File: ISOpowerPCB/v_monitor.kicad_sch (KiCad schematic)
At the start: 26 parts, among them U15 TL431DBZ, U16 TL431DBZ, U17 TL431DBZ, U18 TL431DBZ, U19 HEF4093B

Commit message: PCB Layouts
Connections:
- net 12V_MON_OUT: no longer U19.5, U19.6
- net at D5.2 (A), U19.3: now also U19.5, U19.6; no longer U19.8, U19.9
- net at D6.2 (A), U19.12, U19.13: now also U19.10; no longer U19.4
- net at D7.2 (A): now also U19.4; no longer U19.10
- new net: U19.8, U19.9
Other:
- moved on the sheet: U19B, U19C

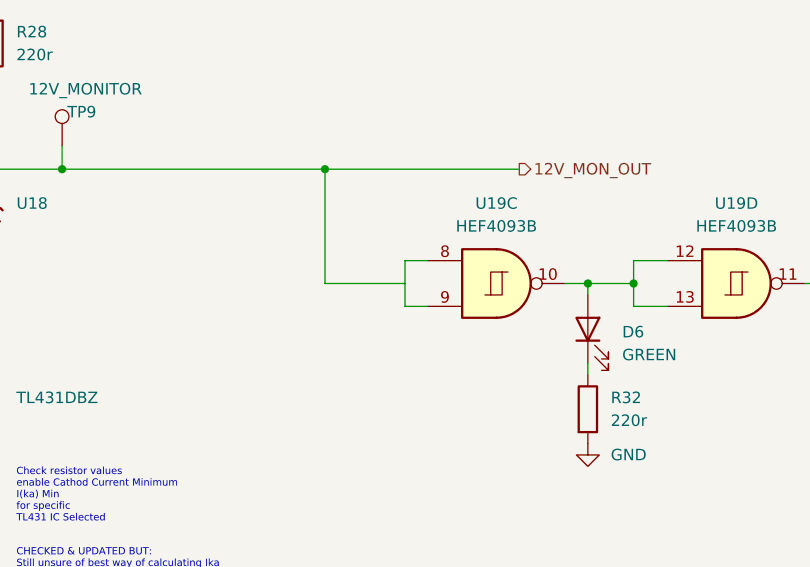
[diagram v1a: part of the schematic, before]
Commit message: Components placed V1.0
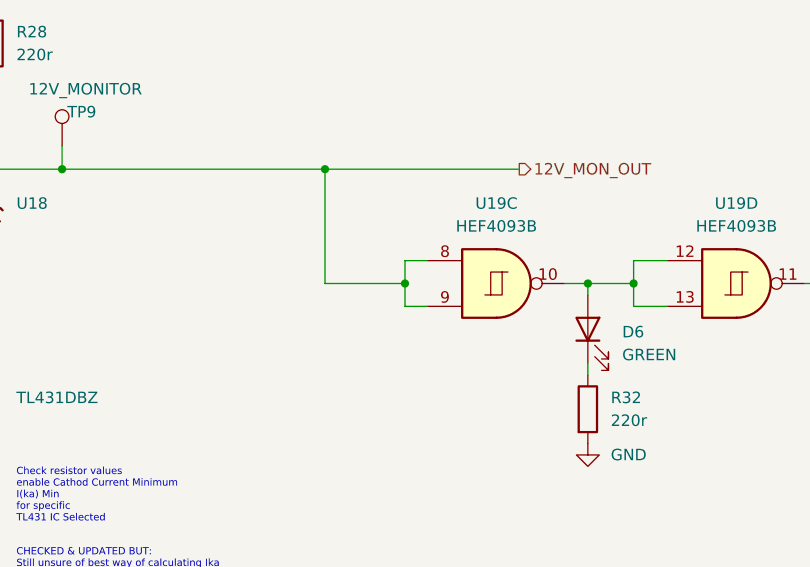
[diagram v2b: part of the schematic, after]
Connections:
- net 12V_MON_OUT: now also U19.8, U19.9
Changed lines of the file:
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@@
   (junction (at 38.1 140.97) (diameter 0) (color 0 0 0 0)
   )
+  (junction (at 119.38 143.51) (diameter 0) (color 0 0 0 0)
+  )
   (wire (pts (xy 228.6 30.48) (xy 231.14 30.48))
     (stroke (width 0) (type default) (color 0 0 0 0))
@@
     (stroke (width 0) (type default) (color 0 0 0 0))
   )
-  (wire (pts (xy 119.38 140.97) (xy 119.38 146.05))
+  (wire (pts (xy 119.38 140.97) (xy 119.38 143.51))
     (stroke (width 0) (type default) (color 0 0 0 0))
   )
@@
     (stroke (width 0) (type default) (color 0 0 0 0))
   )
+  (wire (pts (xy 119.38 143.51) (xy 119.38 146.05))
+    (stroke (width 0) (type default) (color 0 0 0 0))
+  )

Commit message: Started Routing V1
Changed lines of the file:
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@@
       (effects (font (size 1.27 1.27)) (justify right))
     )
-    (property "Value" "TL431DBZ" (id 1) (at 76.2 156.2099 90)
+    (property "Value" "TL431DBZ" (id 1) (at 76.2 137.16 90)
       (effects (font (size 1.27 1.27)) (justify right))
     )

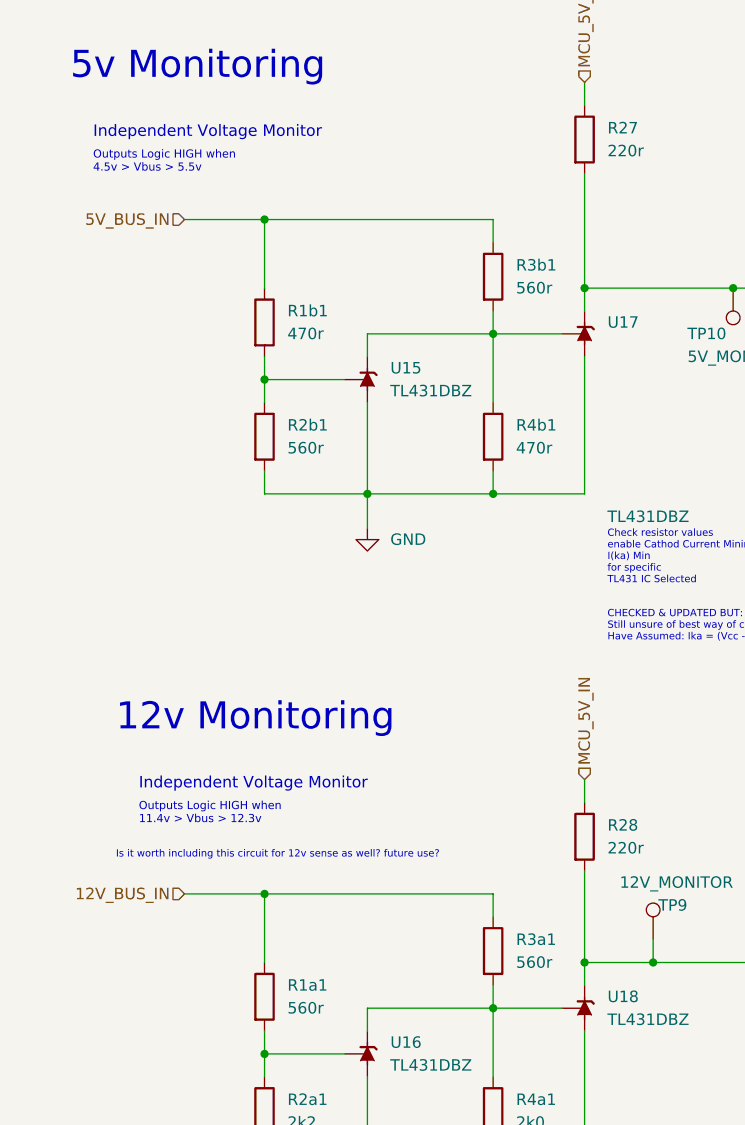
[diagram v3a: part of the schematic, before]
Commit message: Replacing power bus RE current draw issue
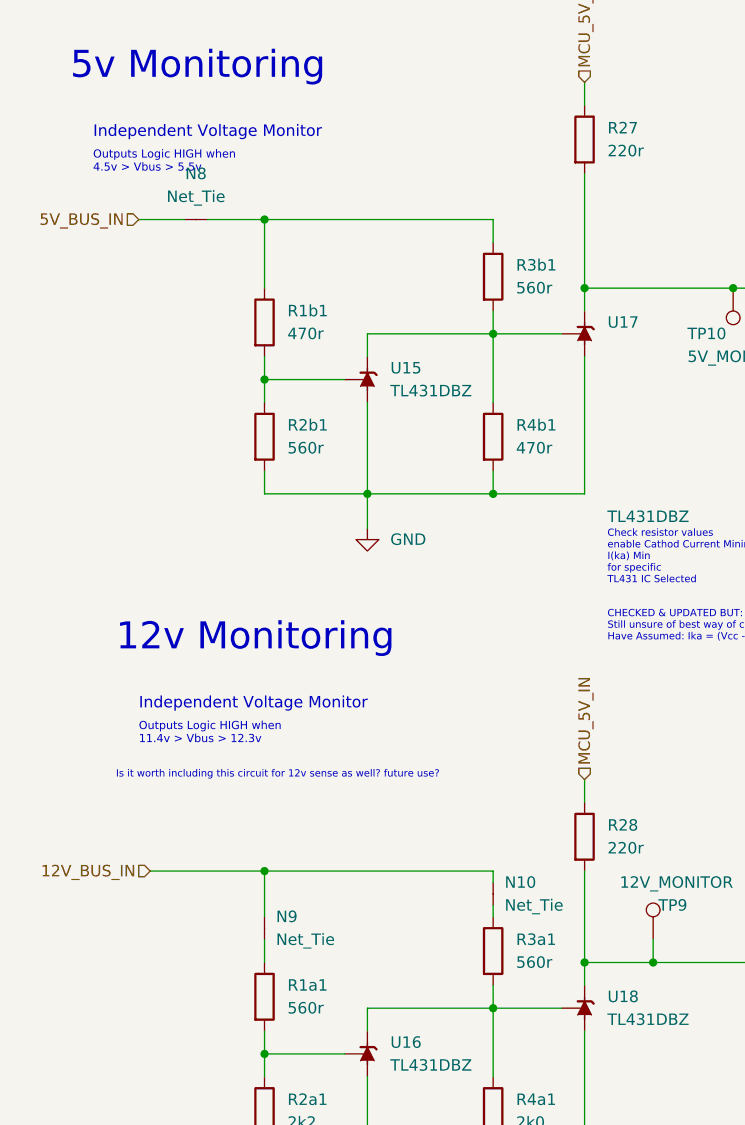
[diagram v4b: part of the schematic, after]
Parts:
- added N10, N8, N9: Net_Tie, NetTie:NetTie-2_SMD_Pad0.5mm, symbol 000_Utility_Immo:Net_Tie
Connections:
- net 12V_BUS_IN: now also N10.1 (A), N9.1 (A); no longer R1a1.1, R3a1.1
- net 5V_BUS_IN: now also N8.1 (A); no longer R1b1.1, R3b1.1
- new net: N9.2 (C), R1a1.1
- new net: N8.2 (C), R1b1.1, R3b1.1
- new net: N10.2 (C), R3a1.1
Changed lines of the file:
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@@
   (junction (at 63.5 135.89) (diameter 0) (color 0 0 0 0)
   )
-  (junction (at 38.1 123.19) (diameter 0) (color 0 0 0 0)
-  )
   (junction (at 63.5 78.74) (diameter 0) (color 0 0 0 0)
   )
@@
   (junction (at 144.78 143.51) (diameter 0) (color 0 0 0 0)
   )
+  (junction (at 38.1 120.65) (diameter 0) (color 0 0 0 0)
+  )
   (junction (at 73.66 55.88) (diameter 0) (color 0 0 0 0)
   )
+  (junction (at 130.81 67.31) (diameter 0) (color 0 0 0 0)
+  )
+  (junction (at 81.28 130.81) (diameter 0) (color 0 0 0 0)
+  )
+  (junction (at 49.53 78.74) (diameter 0) (color 0 0 0 0)
+  )
+  (junction (at 49.53 153.67) (diameter 0) (color 0 0 0 0)
+  )
+  (junction (at 152.4 67.31) (diameter 0) (color 0 0 0 0)
+  )
+  (junction (at 228.6 33.02) (diameter 0) (color 0 0 0 0)
+  )
+  (junction (at 38.1 140.97) (diameter 0) (color 0 0 0 0)
+  )
+  (junction (at 119.38 143.51) (diameter 0) (color 0 0 0 0)
+  )
   (junction (at 38.1 48.26) (diameter 0) (color 0 0 0 0)
   )
-  (junction (at 130.81 67.31) (diameter 0) (color 0 0 0 0)
-  )
-  (junction (at 81.28 130.81) (diameter 0) (color 0 0 0 0)
-  )
-  (junction (at 49.53 78.74) (diameter 0) (color 0 0 0 0)
-  )
-  (junction (at 49.53 153.67) (diameter 0) (color 0 0 0 0)
-  )
-  (junction (at 152.4 67.31) (diameter 0) (color 0 0 0 0)
-  )
-  (junction (at 228.6 33.02) (diameter 0) (color 0 0 0 0)
-  )
-  (junction (at 38.1 140.97) (diameter 0) (color 0 0 0 0)
-  )
-  (junction (at 119.38 143.51) (diameter 0) (color 0 0 0 0)
-  )
   (wire (pts (xy 228.6 30.48) (xy 231.14 30.48))
     (stroke (width 0) (type default) (color 0 0 0 0))
@@
     (stroke (width 0) (type default) (color 0 0 0 0))
   )
+  (wire (pts (xy 24.13 48.26) (xy 29.21 48.26))
+    (stroke (width 0) (type default) (color 0 0 0 0))
+  )
+  (wire (pts (xy 38.1 120.65) (xy 63.5 120.65))
+    (stroke (width 0) (type default) (color 0 0 0 0))
+  )
   (wire (pts (xy 180.34 86.36) (xy 180.34 87.63))
     (stroke (width 0) (type default) (color 0 0 0 0))
@@
     (stroke (width 0) (type default) (color 0 0 0 0))
   )
+  (wire (pts (xy 38.1 128.27) (xy 38.1 130.81))
+    (stroke (width 0) (type default) (color 0 0 0 0))
+  )
   (wire (pts (xy 63.5 135.89) (xy 63.5 143.51))
     (stroke (width 0) (type default) (color 0 0 0 0))
@@
     (stroke (width 0) (type default) (color 0 0 0 0))
   )
+  (wire (pts (xy 63.5 120.65) (xy 63.5 121.92))
+    (stroke (width 0) (type default) (color 0 0 0 0))
+  )
   (wire (pts (xy 49.53 78.74) (xy 49.53 82.55))
     (stroke (width 0) (type default) (color 0 0 0 0))
@@
     (stroke (width 0) (type default) (color 0 0 0 0))
   )
-  (wire (pts (xy 29.21 48.26) (xy 38.1 48.26))
-    (stroke (width 0) (type default) (color 0 0 0 0))
-  )
-  (wire (pts (xy 63.5 125.73) (xy 63.5 123.19))
-    (stroke (width 0) (type default) (color 0 0 0 0))
-  )
   (wire (pts (xy 38.1 138.43) (xy 38.1 140.97))
     (stroke (width 0) (type default) (color 0 0 0 0))
@@
     (stroke (width 0) (type default) (color 0 0 0 0))
   )
+  (wire (pts (xy 38.1 120.65) (xy 38.1 125.73))
+    (stroke (width 0) (type default) (color 0 0 0 0))
+  )
   (wire (pts (xy 148.59 67.31) (xy 152.4 67.31))
     (stroke (width 0) (type default) (color 0 0 0 0))
@@
     (stroke (width 0) (type default) (color 0 0 0 0))
   )
+  (wire (pts (xy 25.4 120.65) (xy 38.1 120.65))
+    (stroke (width 0) (type default) (color 0 0 0 0))
+  )
   (wire (pts (xy 152.4 67.31) (xy 152.4 69.85))
     (stroke (width 0) (type default) (color 0 0 0 0))
@@
     (stroke (width 0) (type default) (color 0 0 0 0))
   )
-  (wire (pts (xy 29.21 123.19) (xy 38.1 123.19))
-    (stroke (width 0) (type default) (color 0 0 0 0))
-  )
   (wire (pts (xy 119.38 143.51) (xy 110.49 143.51))
     (stroke (width 0) (type default) (color 0 0 0 0))
@@
     (stroke (width 0) (type default) (color 0 0 0 0))
   )
-  (wire (pts (xy 63.5 123.19) (xy 38.1 123.19))
-    (stroke (width 0) (type default) (color 0 0 0 0))
-  )
   (wire (pts (xy 73.66 78.74) (xy 63.5 78.74))
     (stroke (width 0) (type default) (color 0 0 0 0))
   )
-  (wire (pts (xy 38.1 123.19) (xy 38.1 130.81))
-    (stroke (width 0) (type default) (color 0 0 0 0))
-  )
   (wire (pts (xy 139.7 152.4) (xy 139.7 153.67))
     (stroke (width 0) (type default) (color 0 0 0 0))
@@
     (stroke (width 0) (type default) (color 0 0 0 0))
   )
+  (wire (pts (xy 31.75 48.26) (xy 38.1 48.26))
+    (stroke (width 0) (type default) (color 0 0 0 0))
+  )
   (wire (pts (xy 228.6 30.48) (xy 228.6 33.02))
     (stroke (width 0) (type default) (color 0 0 0 0))
@@
     (stroke (width 0) (type default) (color 0 0 0 0))
   )
-  (text "Outputs Logic HIGH when\n11.4v > Vbus > 12.3v " (at 24.13 115.57 0)
+  (wire (pts (xy 63.5 124.46) (xy 63.5 125.73))
+    (stroke (width 0) (type default) (color 0 0 0 0))
+  )
+  (text "Outputs Logic HIGH when\n11.4v > Vbus > 12.3v " (at 24.13 106.68 0)
     (effects (font (size 0.9 0.9)) (justify left bottom))
   )
@@
     (effects (font (size 0.8 0.8)) (justify left bottom))
   )
-  (text "12v Monitoring" (at 21.59 105.41 0)
+  (text "12v Monitoring" (at 21.59 96.52 0)
     (effects (font (size 3 3)) (justify left bottom))
   )
-  (text "Independent Voltage Monitor" (at 24.13 111.76 0)
+  (text "Independent Voltage Monitor" (at 24.13 102.87 0)
     (effects (font (size 1.27 1.27)) (justify left bottom))
   )
   (text "Is it worth including this circuit for 12v sense as well? future use?"
-    (at 21.59 119.38 0)
+    (at 21.59 110.49 0)
     (effects (font (size 0.8 0.8)) (justify left bottom))
   )
@@
     (effects (font (size 1.27 1.27)) (justify left))
   )
-  (hierarchical_label "12V_BUS_IN" (shape input) (at 29.21 123.19 180)
+  (hierarchical_label "12V_BUS_IN" (shape input) (at 25.4 120.65 180)
     (effects (font (size 1.27 1.27)) (justify right))
   )
-  (hierarchical_label "5V_BUS_IN" (shape input) (at 29.21 48.26 180)
+  (hierarchical_label "5V_BUS_IN" (shape input) (at 24.13 48.26 180)
     (effects (font (size 1.27 1.27)) (justify right))
   )
@@
   (hierarchical_label "5V_MON_OUT" (shape output) (at 133.35 55.88 0)
     (effects (font (size 1.27 1.27)) (justify left))
+  )
+  (symbol (lib_id "000_Utility_Immo:Net_Tie") (at 38.1 127 270) (unit 1)
+    (in_bom no) (on_board yes) (fields_autoplaced)
+    (property "Reference" "N9" (id 0) (at 39.37 125.7299 90)
+      (effects (font (size 1.27 1.27)) (justify left))
+    )
+    (property "Value" "Net_Tie" (id 1) (at 39.37 128.2699 90)
+      (effects (font (size 1.27 1.27)) (justify left))
+    )
+    (property "Footprint" "NetTie:NetTie-2_SMD_Pad0.5mm" (id 2) (at 35.56 127 0)
+      (effects (font (size 1.27 1.27)) hide)
+    )
+    (property "Datasheet" "~" (id 3) (at 39.37 127 0)
+      (effects (font (size 1.27 1.27)) hide)
+    )
+    (pin "1")
+    (pin "2")
   )
   (symbol (lib_id "Device:LED") (at 152.4 73.66 90) (unit 1)
@@
     (pin "2")
   )
+  (symbol (lib_id "000_Utility_Immo:Net_Tie") (at 63.5 123.19 270) (unit 1)
+    (in_bom no) (on_board yes) (fields_autoplaced)
+    (property "Reference" "N10" (id 0) (at 64.77 121.9199 90)
+      (effects (font (size 1.27 1.27)) (justify left))
+    )
+    (property "Value" "Net_Tie" (id 1) (at 64.77 124.4599 90)
+      (effects (font (size 1.27 1.27)) (justify left))
+    )
+    (property "Footprint" "NetTie:NetTie-2_SMD_Pad0.5mm" (id 2) (at 60.96 123.19 0)
+      (effects (font (size 1.27 1.27)) hide)
+    )
+    (property "Datasheet" "~" (id 3) (at 64.77 123.19 0)
+      (effects (font (size 1.27 1.27)) hide)
+    )
+    (pin "1")
+    (pin "2")
+  )
   (symbol (lib_id "000_Resistors_Immo:Resistor_0805") (at 63.5 129.54 0) (unit 1)
     (in_bom yes) (on_board yes) (fields_autoplaced)
@@
     (pin "1")
   )
+  (symbol (lib_id "000_Utility_Immo:Net_Tie") (at 30.48 48.26 0) (unit 1)
+    (in_bom no) (on_board yes) (fields_autoplaced)
+    (property "Reference" "N8" (id 0) (at 30.48 43.18 0))
+    (property "Value" "Net_Tie" (id 1) (at 30.48 45.72 0))
+    (property "Footprint" "NetTie:NetTie-2_SMD_Pad0.5mm" (id 2) (at 30.48 50.8 0)
+      (effects (font (size 1.27 1.27)) hide)
+    )
+    (property "Datasheet" "~" (id 3) (at 30.48 46.99 0)
+      (effects (font (size 1.27 1.27)) hide)
+    )
+    (pin "1")
+    (pin "2")
+  )
   (symbol (lib_id "power:PWR_FLAG") (at 231.14 30.48 270) (unit 1)
